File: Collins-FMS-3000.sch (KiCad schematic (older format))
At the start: 30 parts, among them J3 Conn_02x04_Odd_Even, U2 MCP23017_SO, U3 MCP23017_SO, U4 IS31FL3733B

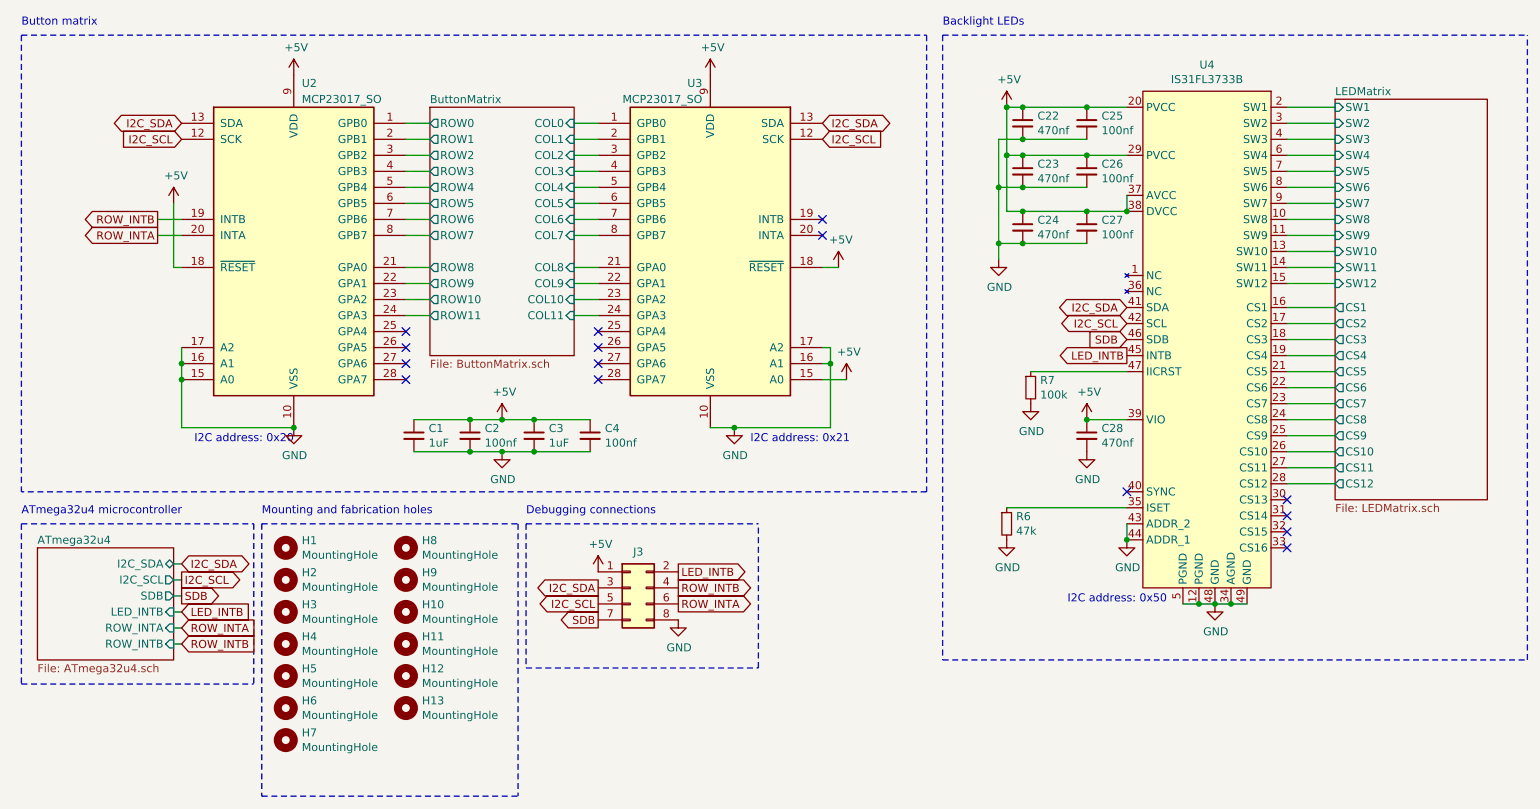
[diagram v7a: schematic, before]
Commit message: More trace routing
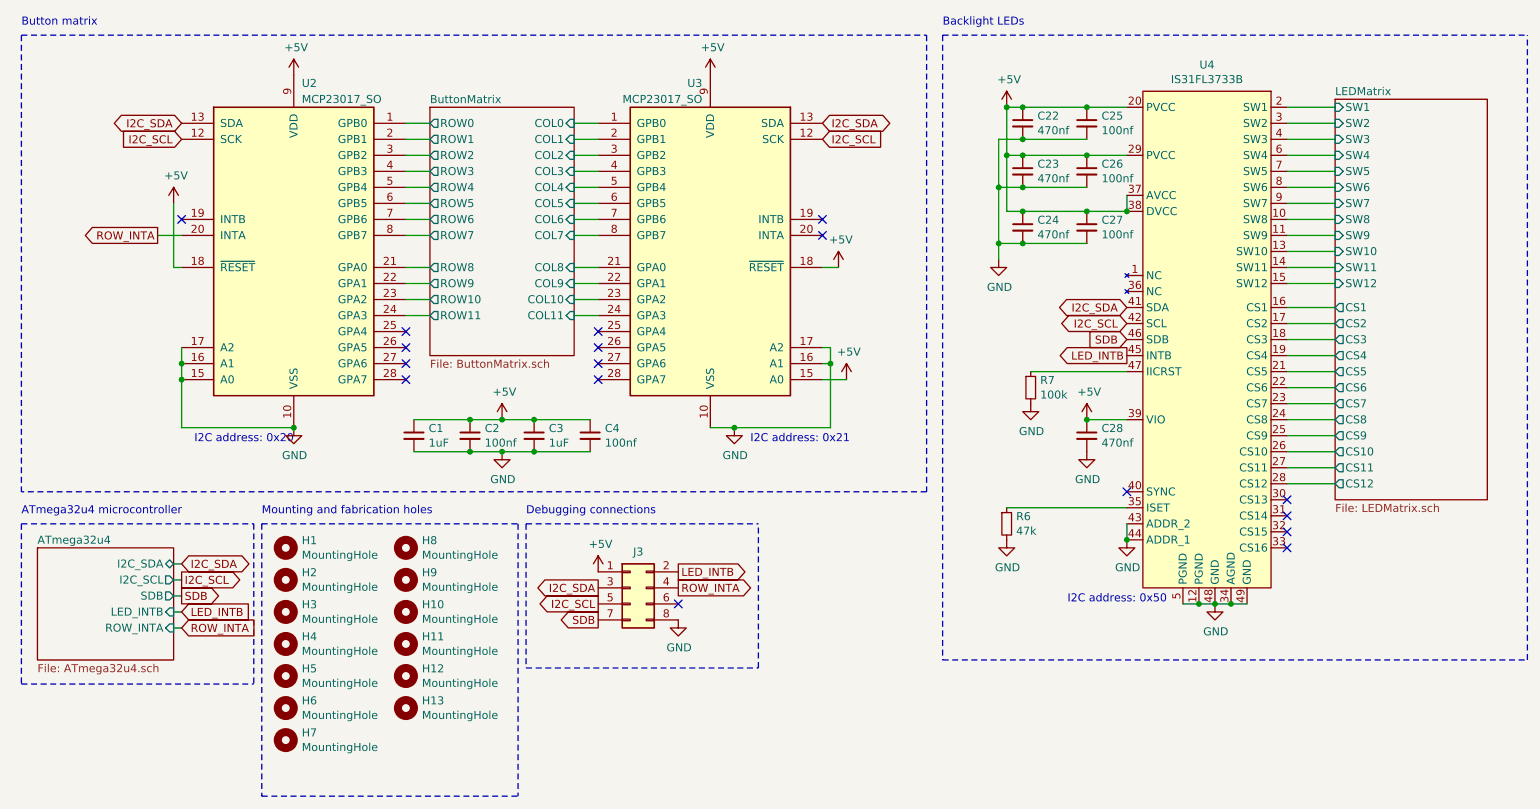
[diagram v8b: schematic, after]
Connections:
- net ROW_INTA: now also J3.4 (Pin_4); no longer J3.6 (Pin_6)
- net ROW_INTB: no longer names the net of U2.19 (INTB)
- net ROW_INTB: no longer J3.4 (Pin_4)
- no-connect marks 15 -> 17
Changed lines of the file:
@@
 F25 "ROW11" O L 3100 2400 50
 $EndSheet
-$Comp
-L Interface_Expansion:MCP23017_SO U2
-U 1 1 626E613B
-P 2250 2000
-F 0 "U2" H 2300 3050 50  0000 L CNN
-F 1 "MCP23017_SO" H 2300 2950 50  0000 L CNN
-F 2 "Package_SO:SOIC-28W_7.5x17.9mm_P1.27mm" H 2450 1000 50  0001 L CNN
-F 3 "http://ww1.microchip.com/downloads/en/DeviceDoc/20001952C.pdf" H 2450 900 50  0001 L CNN
-	1    2250 2000
-	1    0    0    -1
-$EndComp
 Text GLabel 1550 1200 0    50   BiDi ~ 0
 I2C_SDA
@@
 	1    0    0    -1
 $EndComp
-Wire Wire Line
-	1550 2600 1550 2700
-Connection ~ 1550 2700
-Wire Wire Line
-	1550 2700 1550 2800
 Text Notes 2250 3200 2    50   ~ 0
 I2C address: 0x20
@@
 Wire Wire Line
 	5550 2100 5650 2100
-Connection ~ 1550 2800
 Wire Wire Line
 	2250 3100 1550 3100
-Wire Wire Line
-	1550 2800 1550 3100
-Connection ~ 2250 3100
 Text Notes 550  600  0    50   ~ 0
 Button matrix
@@
 F5 "LED_INTB" I R 1500 4250 50
 F6 "ROW_INTA" I R 1500 4350 50
-F7 "ROW_INTB" I R 1500 4450 50
 $EndSheet
 Text GLabel 1550 3950 2    50   BiDi ~ 0
@@
 Wire Wire Line
 	1400 1900 1550 1900
-Wire Wire Line
-	1550 1800 1400 1800
-Text GLabel 1400 1800 0    50   Output ~ 0
-ROW_INTB
 $Comp
 L power:+5V #PWR017
@@
 Text GLabel 4650 4000 2    50   Output ~ 0
 LED_INTB
-Text GLabel 4650 4200 2    50   Output ~ 0
+Text GLabel 4650 4100 2    50   Output ~ 0
 ROW_INTA
-Text GLabel 4650 4100 2    50   Output ~ 0
-ROW_INTB
 $Comp
 L power:GND #PWR019
@@
 Text Notes 3700 3650 0    50   ~ 0
 Debugging connections
-Wire Wire Line
-	1500 4450 1550 4450
-Text GLabel 1550 4450 2    50   Input ~ 0
-ROW_INTB
 Wire Notes Line
 	3700 3700 3700 4600
@@
 Wire Notes Line
 	3700 3700 5150 3700
+Connection ~ 8000 4200
+Connection ~ 7900 4200
+Wire Wire Line
+	8000 4200 8100 4200
+Wire Wire Line
+	7800 4200 7900 4200
+$Comp
+L Collins-FMS-3000:IS31FL3733B U4
+U 1 1 61B33736
+P 7950 2150
+F 0 "U4" H 7950 3465 50  0000 C CNN
+F 1 "IS31FL3733B" H 7950 3374 50  0000 C CNN
+F 2 "Package_QFP:TQFP-48-1EP_7x7mm_P0.5mm_EP5x5mm_ThermalVias" H 7950 -350 50  0001 C CNN
+F 3 "https://www.lumissil.com/assets/pdf/core/IS31FL3733B_DS.pdf" H 7950 2150 50  0001 C CNN
+	1    7950 2150
+	1    0    0    -1
+$EndComp
+Wire Wire Line
+	8200 4200 8100 4200
+Connection ~ 8100 4200
+Wire Wire Line
+	7900 4200 8000 4200
+Connection ~ 7450 3800
+Wire Wire Line
+	7450 3700 7450 3800
+$Comp
+L power:GND #PWR015
+U 1 1 61A9E1C7
+P 7450 3800
+F 0 "#PWR015" H 7450 3550 50  0001 C CNN
+F 1 "GND" H 7455 3627 50  0000 C CNN
+F 2 "" H 7450 3800 50  0001 C CNN
+F 3 "" H 7450 3800 50  0001 C CNN
+	1    7450 3800
+	1    0    0    -1
+$EndComp
+$Comp
+L Mechanical:MountingHole H8
+U 1 1 61AD38B3
+P 2950 3850
+F 0 "H8" H 3050 3896 50  0000 L CNN
+F 1 "MountingHole" H 3050 3805 50  0000 L CNN
+F 2 "MountingHole:MountingHole_3.2mm_M3" H 2950 3850 50  0001 C CNN
+F 3 "~" H 2950 3850 50  0001 C CNN
+	1    2950 3850
+	1    0    0    -1
+$EndComp
+$Comp
+L Mechanical:MountingHole H10
+U 1 1 61AD8E9A
+P 2950 4250
+F 0 "H10" H 3050 4296 50  0000 L CNN
+F 1 "MountingHole" H 3050 4205 50  0000 L CNN
+F 2 "MountingHole:MountingHole_3.2mm_M3" H 2950 4250 50  0001 C CNN
+F 3 "~" H 2950 4250 50  0001 C CNN
+	1    2950 4250
+	1    0    0    -1
+$EndComp
+$Comp
+L Mechanical:MountingHole H12
+U 1 1 61ADE53B
+P 2950 4650
+F 0 "H12" H 3050 4696 50  0000 L CNN
+F 1 "MountingHole" H 3050 4605 50  0000 L CNN
+F 2 "MountingHole:MountingHole_3.2mm_M3" H 2950 4650 50  0001 C CNN
+F 3 "~" H 2950 4650 50  0001 C CNN
+	1    2950 4650
+	1    0    0    -1
+$EndComp
+$Comp
+L Mechanical:MountingHole H9
+U 1 1 61AE9DE8
+P 2950 4050
+F 0 "H9" H 3050 4096 50  0000 L CNN
+F 1 "MountingHole" H 3050 4005 50  0000 L CNN
+F 2 "MountingHole:MountingHole_3.2mm_M3" H 2950 4050 50  0001 C CNN
+F 3 "~" H 2950 4050 50  0001 C CNN
+	1    2950 4050
+	1    0    0    -1
+$EndComp
+$Comp
+L Mechanical:MountingHole H11
+U 1 1 61AE9DEE
+P 2950 4450
+F 0 "H11" H 3050 4496 50  0000 L CNN
+F 1 "MountingHole" H 3050 4405 50  0000 L CNN
+F 2 "MountingHole:MountingHole_3.2mm_M3" H 2950 4450 50  0001 C CNN
+F 3 "~" H 2950 4450 50  0001 C CNN
+	1    2950 4450
+	1    0    0    -1
+$EndComp
+$Comp
+L Mechanical:MountingHole H13
+U 1 1 61AE9DF4
+P 2950 4850
+F 0 "H13" H 3050 4896 50  0000 L CNN
+F 1 "MountingHole" H 3050 4805 50  0000 L CNN
+F 2 "MountingHole:MountingHole_3.2mm_M3" H 2950 4850 50  0001 C CNN
+F 3 "~" H 2950 4850 50  0001 C CNN
+	1    2950 4850
+	1    0    0    -1
+$EndComp
+Wire Notes Line
+	2050 5400 3650 5400
+Wire Notes Line
+	2050 3700 2050 5400
+Wire Notes Line
+	3650 3700 3650 5400
+Wire Wire Line
+	1550 2600 1550 2700
+Connection ~ 1550 2700
+Wire Wire Line
+	1550 2800 1550 3100
+Wire Wire Line
+	1550 2700 1550 2800
+Connection ~ 1550 2800
+Connection ~ 2250 3100
+$Comp
+L Interface_Expansion:MCP23017_SO U2
+U 1 1 626E613B
+P 2250 2000
+F 0 "U2" H 2300 3050 50  0000 L CNN
+F 1 "MCP23017_SO" H 2300 2950 50  0000 L CNN
+F 2 "Package_SO:SOIC-28W_7.5x17.9mm_P1.27mm" H 2450 1000 50  0001 L CNN
+F 3 "http://ww1.microchip.com/downloads/en/DeviceDoc/20001952C.pdf" H 2450 900 50  0001 L CNN
+	1    2250 2000
+	1    0    0    -1
+$EndComp
+NoConn ~ 1550 1800
 $Comp
 L Connector_Generic:Conn_02x04_Odd_Even J3
@@
 	1    0    0    -1
 $EndComp
-Connection ~ 8000 4200
-Connection ~ 7900 4200
-Wire Wire Line
-	8000 4200 8100 4200
-Wire Wire Line
-	7800 4200 7900 4200
-$Comp
-L Collins-FMS-3000:IS31FL3733B U4
-U 1 1 61B33736
-P 7950 2150
-F 0 "U4" H 7950 3465 50  0000 C CNN
-F 1 "IS31FL3733B" H 7950 3374 50  0000 C CNN
-F 2 "Package_QFP:TQFP-48-1EP_7x7mm_P0.5mm_EP5x5mm_ThermalVias" H 7950 -350 50  0001 C CNN
-F 3 "https://www.lumissil.com/assets/pdf/core/IS31FL3733B_DS.pdf" H 7950 2150 50  0001 C CNN
-	1    7950 2150
-	1    0    0    -1
-$EndComp
-Wire Wire Line
-	8200 4200 8100 4200
-Connection ~ 8100 4200
-Wire Wire Line
-	7900 4200 8000 4200
-Connection ~ 7450 3800
-Wire Wire Line
-	7450 3700 7450 3800
-$Comp
-L power:GND #PWR015
-U 1 1 61A9E1C7
-P 7450 3800
-F 0 "#PWR015" H 7450 3550 50  0001 C CNN
-F 1 "GND" H 7455 3627 50  0000 C CNN
-F 2 "" H 7450 3800 50  0001 C CNN
-F 3 "" H 7450 3800 50  0001 C CNN
-	1    7450 3800
-	1    0    0    -1
-$EndComp
-$Comp
-L Mechanical:MountingHole H8
-U 1 1 61AD38B3
-P 2950 3850
-F 0 "H8" H 3050 3896 50  0000 L CNN
-F 1 "MountingHole" H 3050 3805 50  0000 L CNN
-F 2 "MountingHole:MountingHole_3.2mm_M3" H 2950 3850 50  0001 C CNN
-F 3 "~" H 2950 3850 50  0001 C CNN
-	1    2950 3850
-	1    0    0    -1
-$EndComp
-$Comp
-L Mechanical:MountingHole H10
-U 1 1 61AD8E9A
-P 2950 4250
-F 0 "H10" H 3050 4296 50  0000 L CNN
-F 1 "MountingHole" H 3050 4205 50  0000 L CNN
-F 2 "MountingHole:MountingHole_3.2mm_M3" H 2950 4250 50  0001 C CNN
-F 3 "~" H 2950 4250 50  0001 C CNN
-	1    2950 4250
-	1    0    0    -1
-$EndComp
-$Comp
-L Mechanical:MountingHole H12
-U 1 1 61ADE53B
-P 2950 4650
-F 0 "H12" H 3050 4696 50  0000 L CNN
-F 1 "MountingHole" H 3050 4605 50  0000 L CNN
-F 2 "MountingHole:MountingHole_3.2mm_M3" H 2950 4650 50  0001 C CNN
-F 3 "~" H 2950 4650 50  0001 C CNN
-	1    2950 4650
-	1    0    0    -1
-$EndComp
-$Comp
-L Mechanical:MountingHole H9
-U 1 1 61AE9DE8
-P 2950 4050
-F 0 "H9" H 3050 4096 50  0000 L CNN
-F 1 "MountingHole" H 3050 4005 50  0000 L CNN
-F 2 "MountingHole:MountingHole_3.2mm_M3" H 2950 4050 50  0001 C CNN
-F 3 "~" H 2950 4050 50  0001 C CNN
-	1    2950 4050
-	1    0    0    -1
-$EndComp
-$Comp
-L Mechanical:MountingHole H11
-U 1 1 61AE9DEE
-P 2950 4450
-F 0 "H11" H 3050 4496 50  0000 L CNN
-F 1 "MountingHole" H 3050 4405 50  0000 L CNN
-F 2 "MountingHole:MountingHole_3.2mm_M3" H 2950 4450 50  0001 C CNN
-F 3 "~" H 2950 4450 50  0001 C CNN
-	1    2950 4450
-	1    0    0    -1
-$EndComp
-$Comp
-L Mechanical:MountingHole H13
-U 1 1 61AE9DF4
-P 2950 4850
-F 0 "H13" H 3050 4896 50  0000 L CNN
-F 1 "MountingHole" H 3050 4805 50  0000 L CNN
-F 2 "MountingHole:MountingHole_3.2mm_M3" H 2950 4850 50  0001 C CNN
-F 3 "~" H 2950 4850 50  0001 C CNN
-	1    2950 4850
-	1    0    0    -1
-$EndComp
-Wire Notes Line
-	2050 5400 3650 5400
-Wire Notes Line
-	2050 3700 2050 5400
-Wire Notes Line
-	3650 3700 3650 5400
+NoConn ~ 4650 4200
 $EndSCHEMATC
